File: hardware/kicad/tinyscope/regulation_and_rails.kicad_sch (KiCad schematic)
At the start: 28 parts, among them U5 TPS63802DLAR, U6 TPS63802DLAR, U7 LM27761, U8 REF3030, U9 ADP7142

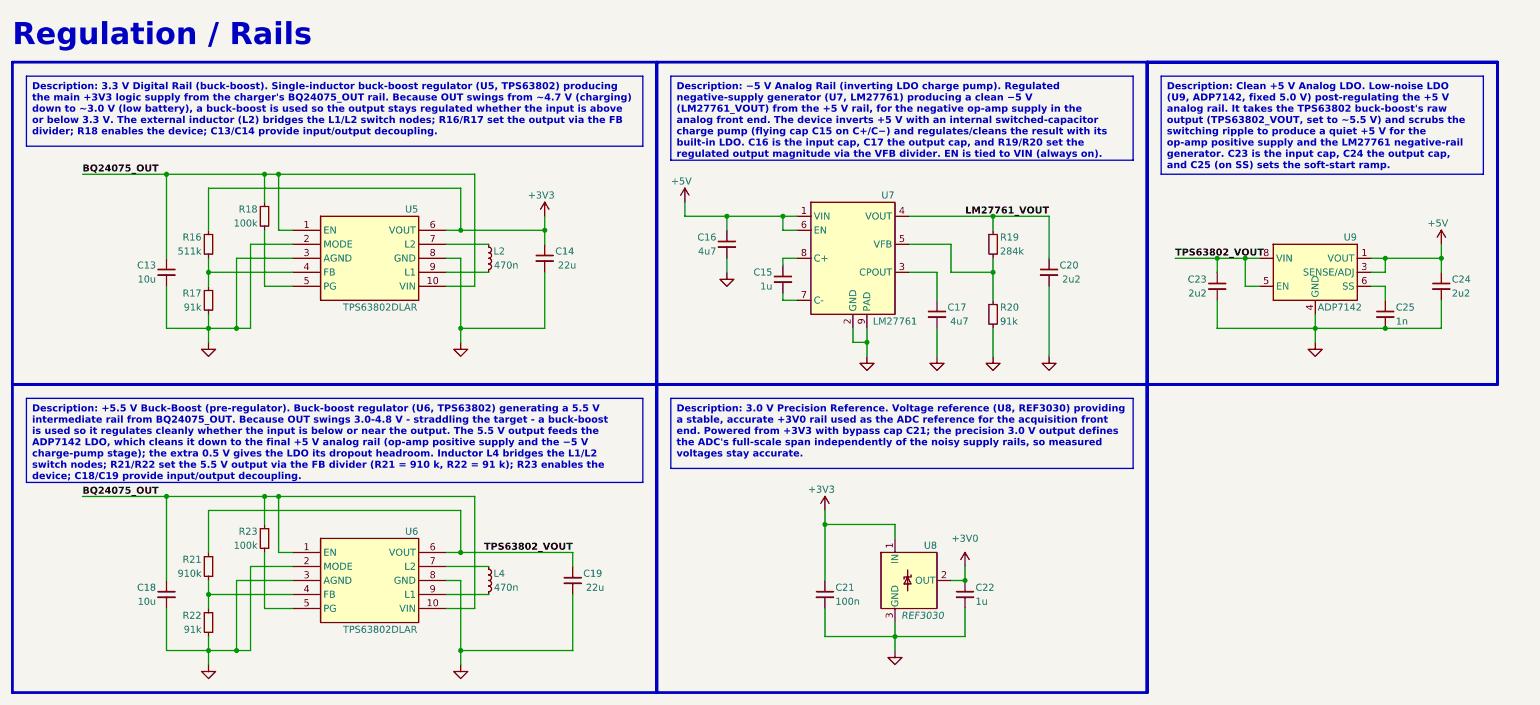
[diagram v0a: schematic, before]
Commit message: feat: hardware: Add tinyscope kicad project. Create flow diagram for Regulation & Rails schemat
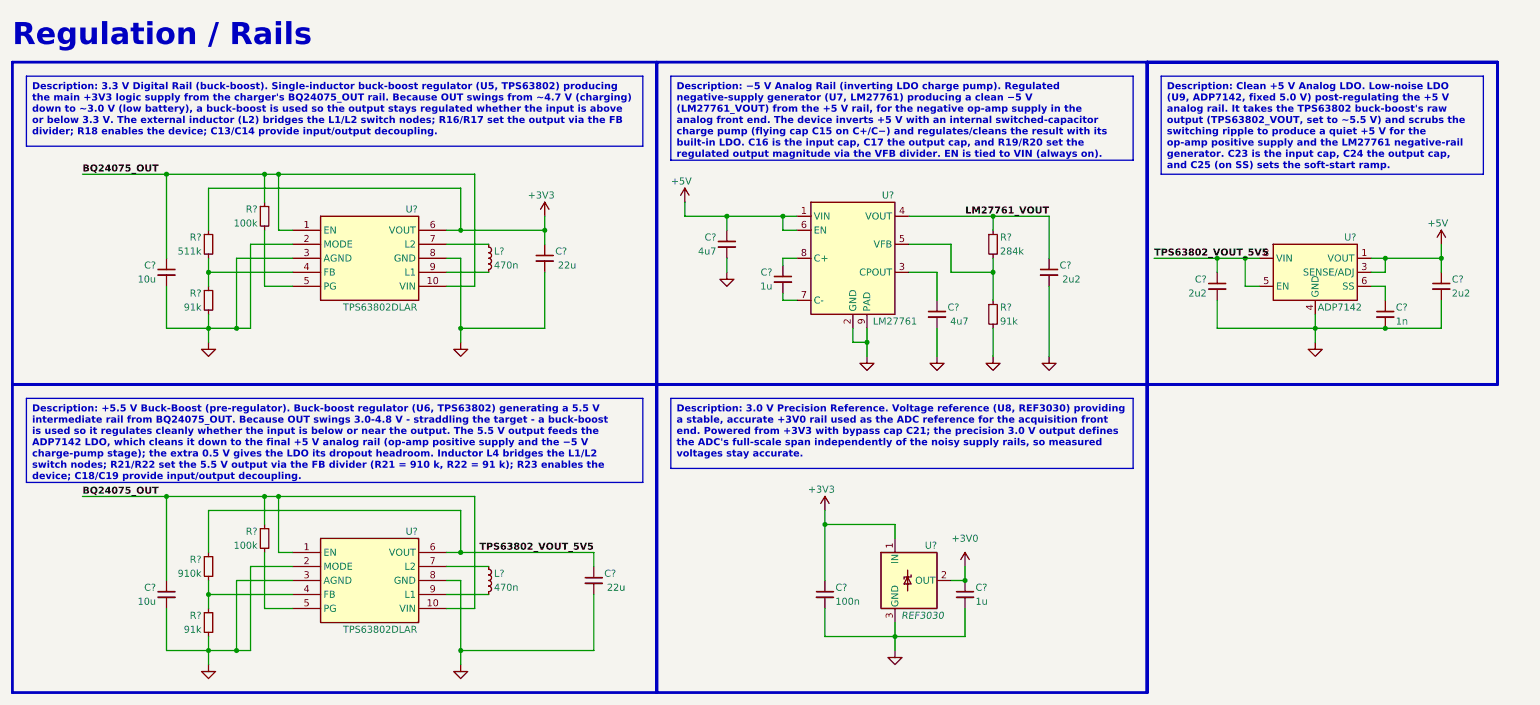
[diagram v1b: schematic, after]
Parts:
- renumbered C15 to C?, C14 to C?, C20 to C?, C16 to C?, C21 to C?, C13 to C?, C18 to C?, C22 to C?, C23 to C?, C19 to C?, C24 to C?, C17 to C?, C25 to C?, L4 to L?, L2 to L?, R19 to R?, R22 to R?, R23 to R?, R21 to R?, R16 to R?, R20 to R?, R18 to R?, R17 to R?, U8 to U?, U7 to U?, U6 to U?, U5 to U?, U9 to U?
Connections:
- net TPS63802_VOUT renamed TPS63802_VOUT_5V5
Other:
- moved on the sheet: C?

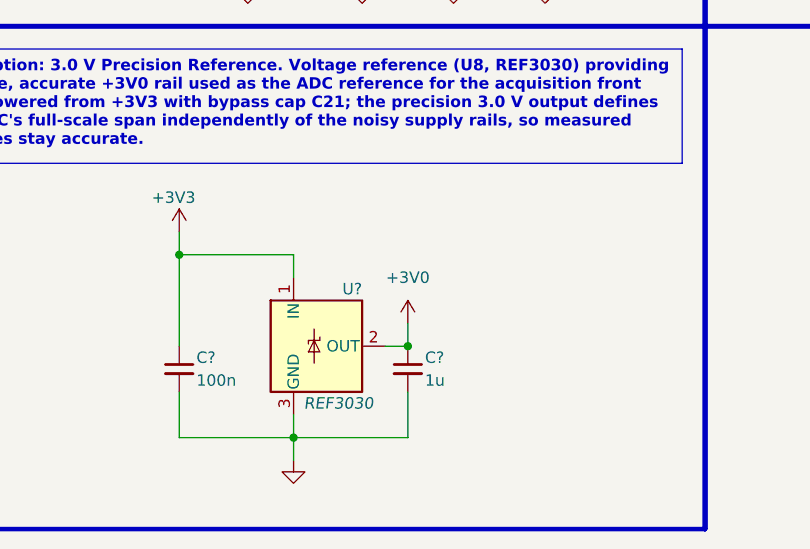
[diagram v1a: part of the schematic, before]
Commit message: feat: hardware: Add tinyscope kicad project. Create flow diagram for MCUs sheet. Adds decoupling caps for STM32H743
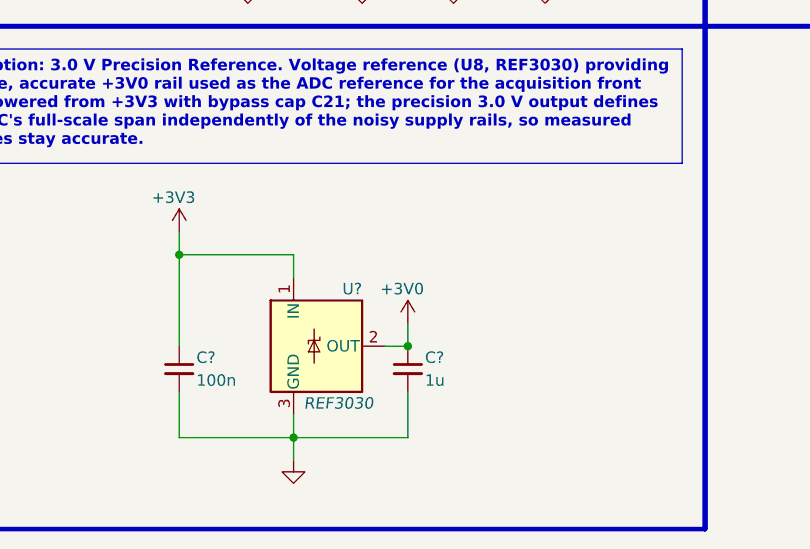
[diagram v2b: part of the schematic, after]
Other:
- title: (none) -> Regulation / Rails
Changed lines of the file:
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@@
 (kicad_sch (version 20230121) (generator eeschema)
   (paper "A4")
+  (title_block
+    (title "Regulation / Rails")
+    (date "2026-06-13")
+    (rev "v0.1")
+  )
   (junction (at 232.41 58.42) (diameter 0) (color 0 0 0 0)
   )
@@
   )
   (symbol (lib_id "power:+3V0") (at 186.69 114.3 0) (unit 1)
-    (in_bom yes) (on_board yes) (dnp no) (fields_autoplaced)
+    (in_bom yes) (on_board yes) (dnp no)
     (property "Reference" "#PWR?" (at 186.69 118.11 0)
       (effects (font (size 1.27 1.27)) hide)
     )
-    (property "Value" "+3V0" (at 186.69 109.22 0)
+    (property "Value" "+3V0" (at 186.055 110.49 0)
       (effects (font (size 1.27 1.27)))
     )
